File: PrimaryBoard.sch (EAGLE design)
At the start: 42 parts, among them J10 LORA32U4II, J11 CONN_42.54_SCREW, J13 POWER_JACK, J4 CONN_32.54_SCREW, J5 CONN_32.54_SCREW, J6 CONN_32.54_SCREW, J7 CONN_32.54_SCREW, J8 CONN_32.54_SCREW, J9 CONN_32.54_SCREW, U1 CD74HC4052PW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

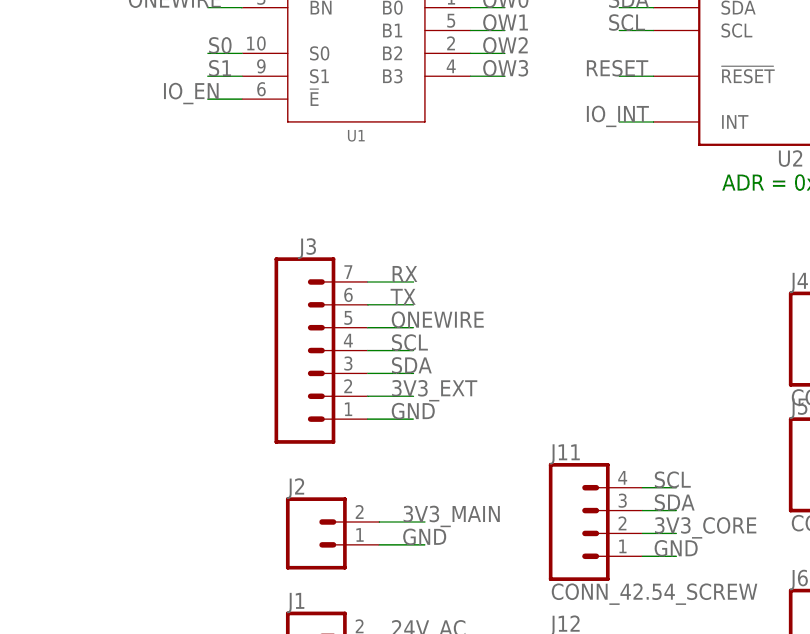
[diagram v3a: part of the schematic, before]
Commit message: Minor updates, part vals
Changed 1x7 connector on Primary board to 1x4 and 1x3 because 1x7 0.1" screw terminals are made of Corinthian Leather apparently, also updated part values and BoM vals
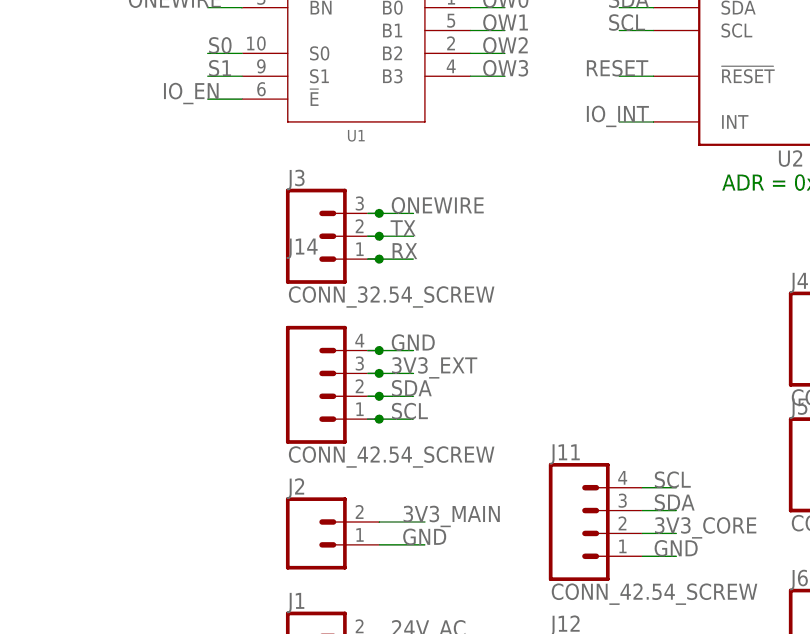
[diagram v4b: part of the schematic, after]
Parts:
- added J14: CONN_42.54_SCREW, bschulz:CONN_42.54_SCREW
- C2: device bschulz_passives:C-EUC0805 -> bschulz_passives:C-EU0.33UFC0805
- C3, C6, C7, C8: device bschulz_passives:C-EUC0805 -> bschulz_passives:C-EU0.1UFC0805
- C4, C5: device bschulz_passives:C-EUC0805 -> bschulz_passives:C-EU1UFC0805
- J3: value (none) -> CONN_32.54_SCREW; device bschulz:CONN_07SCREW_2.54 -> bschulz:CONN_32.54_SCREW
- R1: device bschulz_passives:R-EU_R0805 -> bschulz_passives:R-EU_100KR0805
- R2, R3: device bschulz_passives:R-EU_R0805 -> bschulz_passives:R-EU_10KR0805
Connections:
- net 3V3_EXT: now also J14.3; no longer J3.2
- net GND: now also J14.4; no longer J3.1
- net ONEWIRE: now also J3.3; no longer J3.5
- net RX: now also J3.1; no longer J3.7
- net SCL: now also J14.1; no longer J3.4
- net SDA: now also J14.2; no longer J3.3
- net TX: now also J3.2; no longer J3.6
